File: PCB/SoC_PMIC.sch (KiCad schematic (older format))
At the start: 21 parts

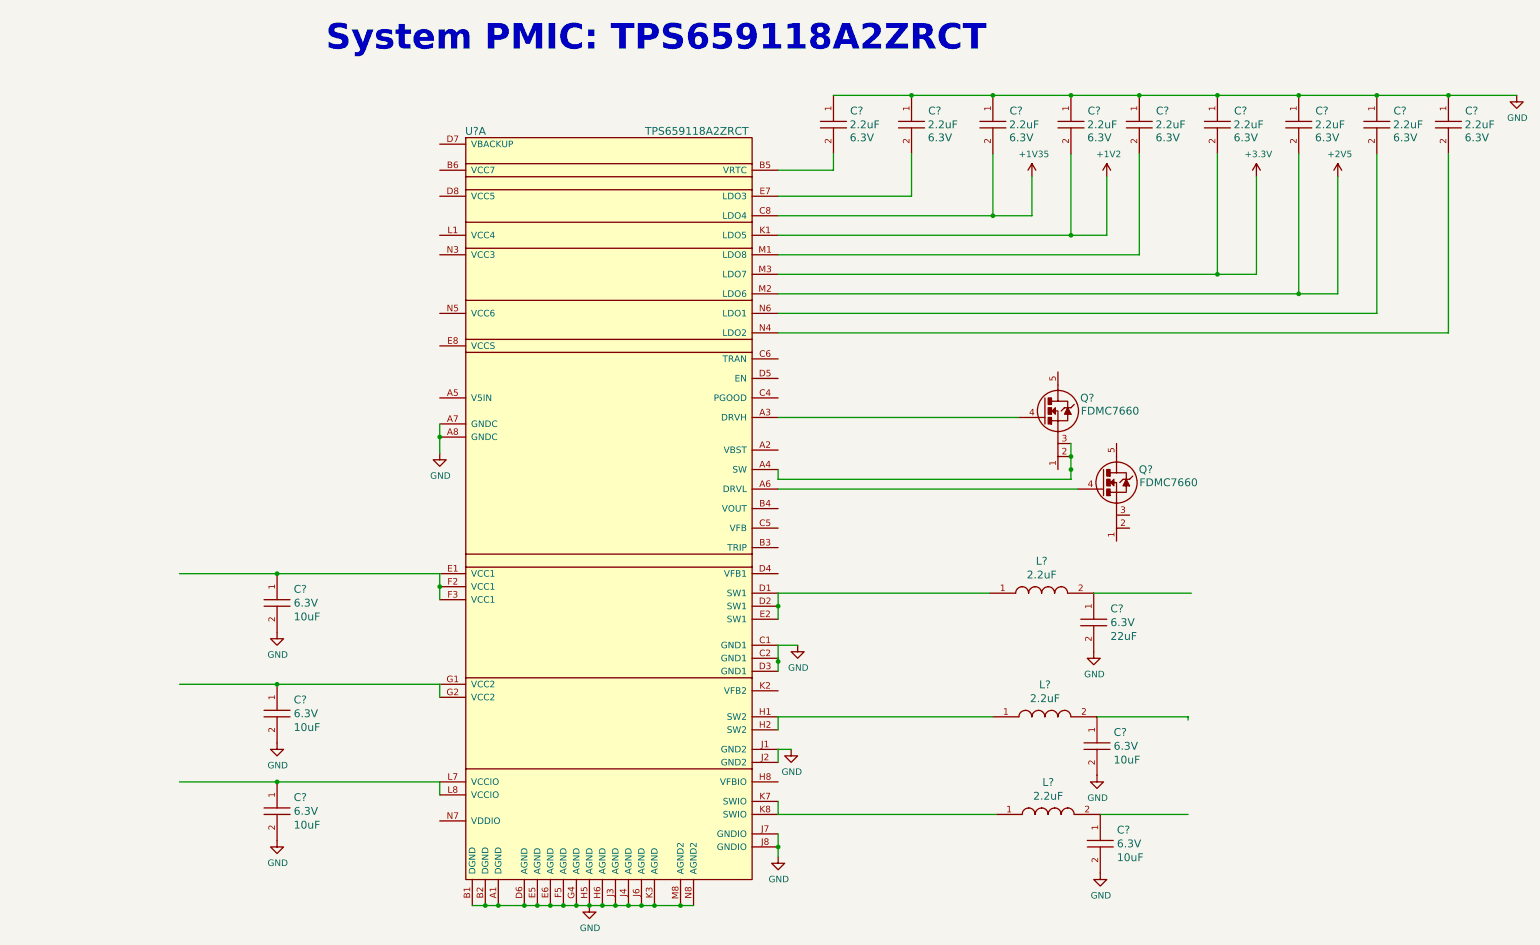
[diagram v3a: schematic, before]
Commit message: PMIC progress
More progress made on the implemenation of the PMIC schematic from the
Ti reference notes. Currently researching a 5V DCDC and input power
circuit that can switch between USB bus power and external power.
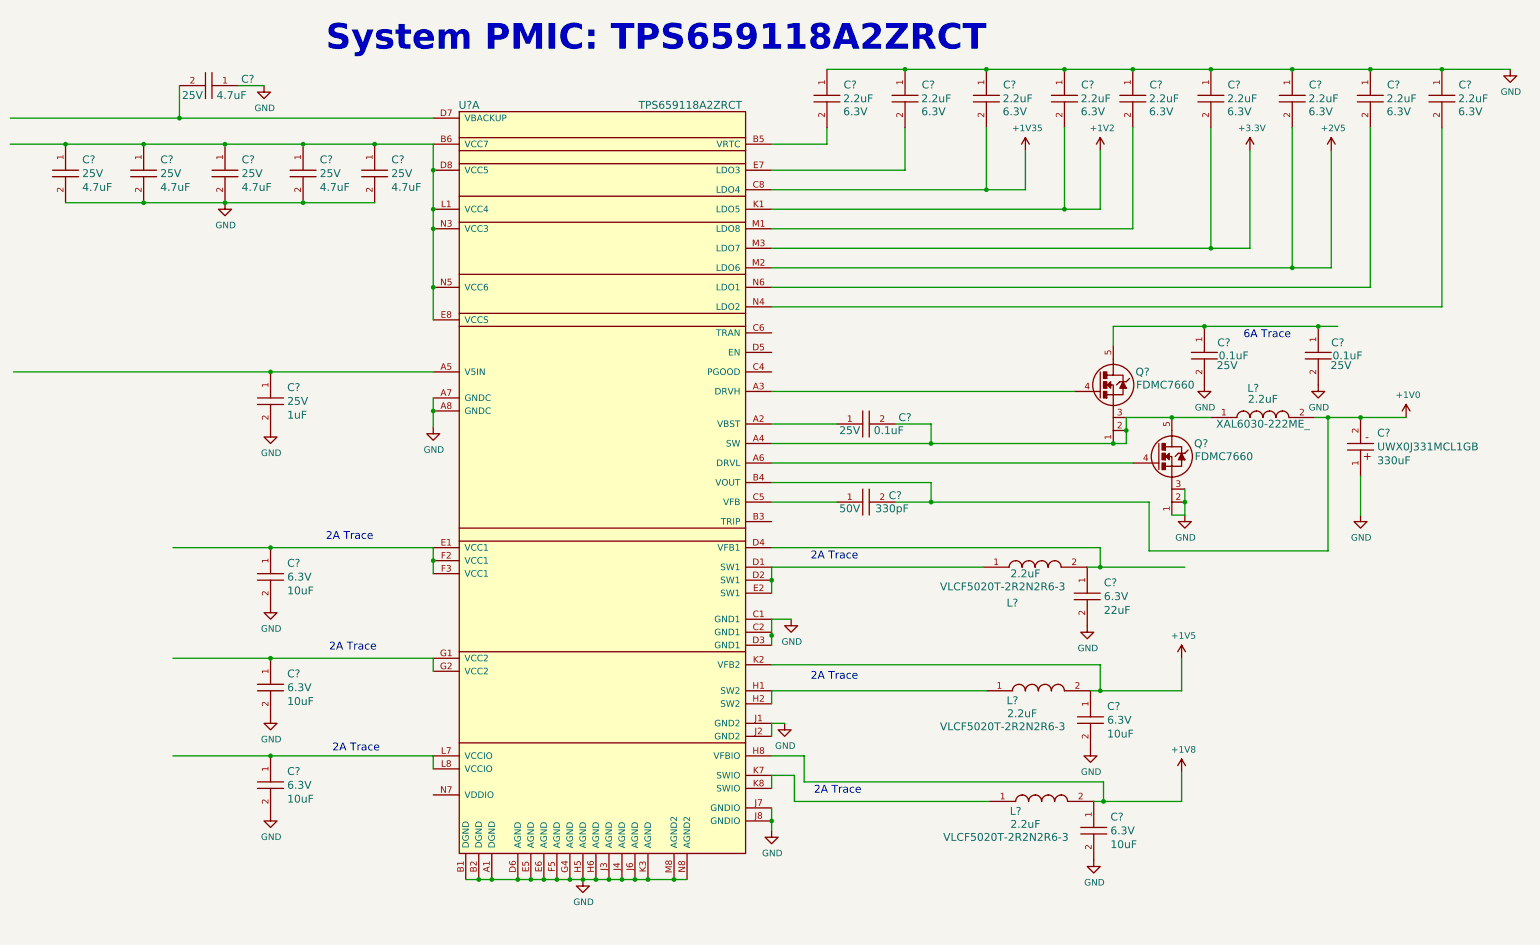
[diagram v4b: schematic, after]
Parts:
- added C? (x3): 08053C104JAT2A, PCB_Footprints:C0805, symbol 08053C104JAT2A
- added C?: GRM1555C1H331FA01J, PCB_Footprints:C0402, symbol GRM1555C1H331FA01J
- added C?: UWX0J331MCL1GB, PCB_Footprints:UWX0J331MCL1GB, symbol UWX0J331MCL1GB
- added C? (x6): CL05A475KQ5NRNC, PCB_Footprints:C0402, symbol CL05A475KQ5NRNC
- added C?: CL05A105KA5NQNC, PCB_Footprints:C0402, symbol CL05A105KA5NQNC
- added L?: XAL6030-222ME_, PCB_Footprints:XAL6030-222ME_, symbol XAL6030-222ME_
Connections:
- net labels added: +1V0, +1V5, +1V8
- wire segments 89 -> 86
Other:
- note added: "2A Trace"
- note added: "6A Trace"
- moved on the sheet: C?, L?, Q?, U?A

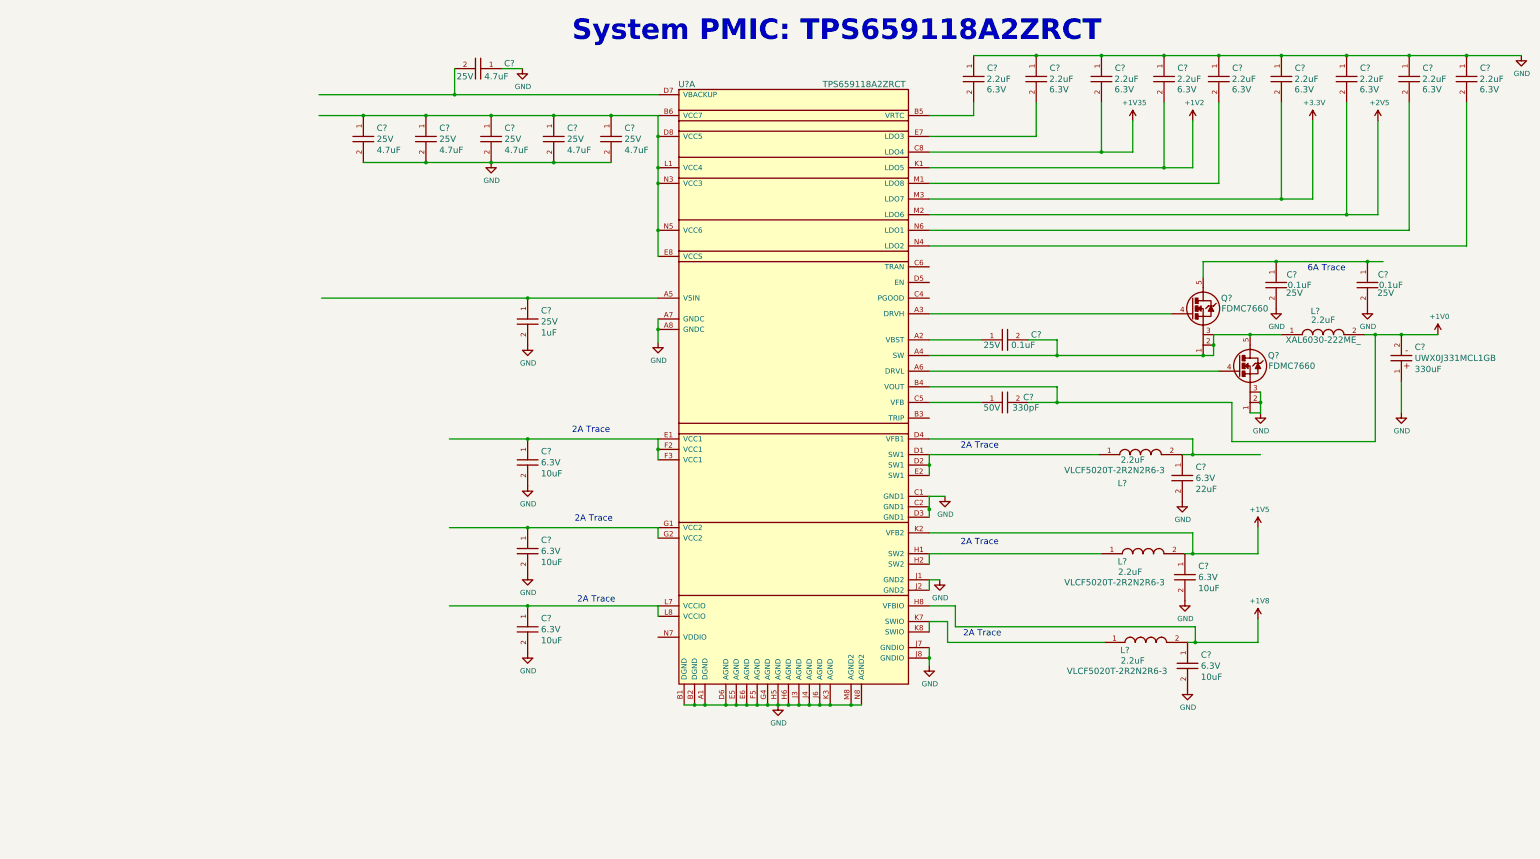
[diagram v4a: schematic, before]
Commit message: Schematic Progress
More progress on schematic. Image sensor schematic nearly finished, need
to check termination requirements of signals. Memory schematic nearly
solidified. LDO added to image sensor circuit for analog supply (3V).
Need to research termination requirements for memory as well. Need to
check what internal termination if any resistors are available in the
Zynq soc.
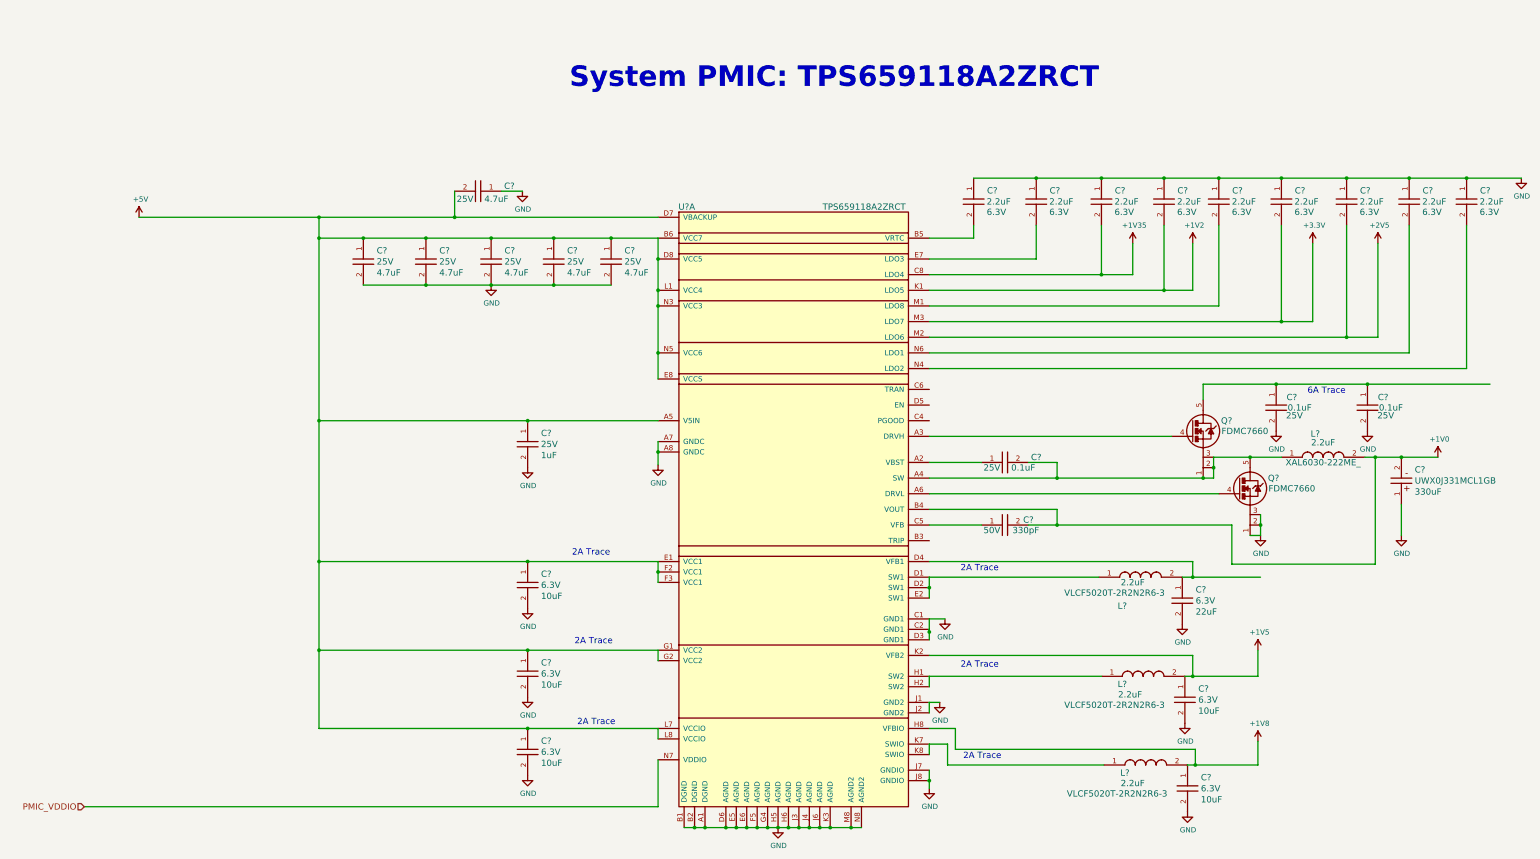
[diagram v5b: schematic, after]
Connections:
- net labels added: +5V, PMIC_VDDIO
- wire segments 86 -> 155
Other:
- moved on the sheet: C?, L?, Q?, U?A

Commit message: USB
This commit contains mostly work done to the USB sections. Theres a FTDI
chip for USB coms and programmign and an USB transceiver/PHY for usb
perfipherals or daisychaining devices.  Also the termiantion resistors
have been removed from the memory since termination can be set on DDR
pins of the FPGA with verilog.
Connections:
- net VCCPINT_1V0: now reaches C?.1, L?.2, U?.D4 (VFB1)
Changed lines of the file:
@@
 $Descr B 17000 11000
 encoding utf-8
-Sheet 7 8
+Sheet 7 10
 Title ""
 Date ""
@@
 $EndComp
 Wire Wire Line
-	6950 8425 7050 8425
-Wire Wire Line
-	7050 8425 7150 8425
-Wire Wire Line
-	7150 8425 7350 8425
-Wire Wire Line
-	7350 8425 7450 8425
-Wire Wire Line
-	7450 8425 7550 8425
-Wire Wire Line
-	7550 8425 7650 8425
-Wire Wire Line
-	7650 8425 7750 8425
-Wire Wire Line
-	7750 8425 7850 8425
-Wire Wire Line
-	7850 8425 7950 8425
-Wire Wire Line
-	7950 8425 8050 8425
-Wire Wire Line
-	8050 8425 8150 8425
-Wire Wire Line
-	8150 8425 8250 8425
-Wire Wire Line
-	8250 8425 8350 8425
-Wire Wire Line
-	8350 8425 8550 8425
-Wire Wire Line
-	8550 8425 8650 8425
+	6950 8425 8650 8425
 Connection ~ 7050 8425
 Connection ~ 7150 8425
@@
 Connection ~ 8550 8425
 Wire Wire Line
-	9300 7875 9300 7975
-Wire Wire Line
-	9300 7975 9300 8050
+	9300 7875 9300 8050
 Wire Wire Line
 	9300 7325 9300 7225
 Wire Wire Line
-	9300 6525 9300 6550
-Wire Wire Line
-	9300 6550 9300 6625
+	9300 6525 9300 6625
 Wire Wire Line
 	9300 6550 9300 6425
 Connection ~ 9300 6550
 Wire Wire Line
-	6700 4725 6700 4825
-Wire Wire Line
-	6700 4825 6700 4950
+	6700 4725 6700 4950
 $Comp
 L GND #PWR?
@@
 	9475 7825 10975 7825
 Wire Wire Line
-	9300 6025 9300 6125
-Wire Wire Line
-	9300 6125 9300 6225
+	9300 6025 9300 6225
 Connection ~ 9300 6125
 Wire Wire Line
 	9300 6025 10925 6025
 Wire Wire Line
-	12025 5075 11925 5075
-Wire Wire Line
-	11925 5075 10525 5075
-Wire Wire Line
-	10525 5075 9300 5075
+	12025 5075 9300 5075
 Text Notes 5850 1350 0    197  ~ 39
 System PMIC: TPS659118A2ZRCT
 Wire Wire Line
-	6700 5875 6700 5975
-Wire Wire Line
-	6700 5975 6700 6075
+	6700 5875 6700 6075
 Connection ~ 6700 5975
 Wire Wire Line
@@
 	6700 7475 6700 7575
 Wire Wire Line
-	3450 7475 5450 7475
-Wire Wire Line
-	5450 7475 6700 7475
-Wire Wire Line
-	3450 6725 5450 6725
-Wire Wire Line
-	5450 6725 6700 6725
-Wire Wire Line
-	3450 5875 5450 5875
-Wire Wire Line
-	5450 5875 6700 5875
+	3450 7475 6700 7475
+Wire Wire Line
+	3450 6725 6700 6725
+Wire Wire Line
+	3450 5875 6700 5875
 $Comp
 L CL10A225KQ8NNNC C?
@@
 	10325 2975 10325 2650
 Wire Wire Line
-	9300 3125 10950 3125
-Wire Wire Line
-	10950 3125 11250 3125
+	9300 3125 11250 3125
 Wire Wire Line
 	10950 3125 10950 2650
 Wire Wire Line
-	9300 3275 11550 3275
-Wire Wire Line
-	11550 3275 11825 3275
+	9300 3275 11825 3275
 Wire Wire Line
 	11550 3275 11550 2650
@@
 	12075 3425 12075 2650
 Wire Wire Line
-	9300 3575 12675 3575
-Wire Wire Line
-	12675 3575 12975 3575
+	9300 3575 12975 3575
 Wire Wire Line
 	12675 3575 12675 2650
 Wire Wire Line
-	9300 3725 13300 3725
-Wire Wire Line
-	13300 3725 13600 3725
+	9300 3725 13600 3725
 Wire Wire Line
 	13300 3725 13300 2650
@@
 	14450 4025 14450 2650
 Wire Wire Line
-	9725 2200 10325 2200
-Wire Wire Line
-	10325 2200 10950 2200
-Wire Wire Line
-	10950 2200 11550 2200
-Wire Wire Line
-	11550 2200 12075 2200
-Wire Wire Line
-	12075 2200 12675 2200
-Wire Wire Line
-	12675 2200 13300 2200
-Wire Wire Line
-	13300 2200 13900 2200
-Wire Wire Line
-	13900 2200 14450 2200
-Wire Wire Line
-	14450 2200 14975 2200
+	9725 2200 14975 2200
 Connection ~ 13900 2200
 Connection ~ 13300 2200
@@
 L GND #PWR?
 U 1 1 588BD4D5
-P 14975 2200
-F 0 "#PWR?" H 14975 1950 50  0001 C CNN
-F 1 "GND" H 14980 2027 50  0000 C CNN
-F 2 "" H 14975 2200 50  0001 C CNN
-F 3 "" H 14975 2200 50  0001 C CNN
-	1    14975 2200
+P 14975 2700
+F 0 "#PWR?" H 14975 2450 50  0001 C CNN
+F 1 "GND" H 14980 2527 50  0000 C CNN
+F 2 "" H 14975 2700 50  0001 C CNN
+F 3 "" H 14975 2700 50  0001 C CNN
+	1    14975 2700
 	1    0    0    -1
 $EndComp
@@
 $EndComp
 Wire Wire Line
-	11725 6025 11825 6025
-Wire Wire Line
-	11825 6025 12475 6025
-Wire Wire Line
-	11750 6975 11825 6975
-Wire Wire Line
-	11825 6975 12450 6975
-Wire Wire Line
-	11775 7825 11850 7825
-Wire Wire Line
-	11850 7825 12450 7825
+	11725 6025 15400 6025
+Wire Wire Line
+	11750 6975 12450 6975
+Wire Wire Line
+	11775 7825 12450 7825
 $Comp
 L GND #PWR?
@@
 	9300 5225 12075 5225
 Wire Wire Line
-	12025 4875 12025 4975
-Wire Wire Line
-	12025 4975 12025 5075
+	12025 4875 12025 5075
 Connection ~ 12025 4975
 Wire Wire Line
-	12025 4875 12375 4875
-Wire Wire Line
-	12375 4875 12675 4875
+	12025 4875 12675 4875
 Connection ~ 11925 5075
 Wire Wire Line
 	12475 5625 12375 5625
 Wire Wire Line
-	12475 5425 12475 5525
-Wire Wire Line
-	12475 5525 12475 5625
+	12475 5425 12475 5625
 Connection ~ 12475 5525
 $Comp
@@
 	10525 5375 10525 5525
 Wire Wire Line
-	10250 5525 10525 5525
-Wire Wire Line
-	10525 5525 12200 5525
+	10250 5525 12200 5525
 Wire Wire Line
 	12200 5525 12200 5900
@@
 	13575 5900 13575 4875
 Wire Wire Line
-	13475 4875 13575 4875
-Wire Wire Line
-	13575 4875 13825 4875
-Wire Wire Line
-	13825 4875 14175 4875
+	13475 4875 14175 4875
 $Comp
 L GRM1555C1H331FA01J C?
@@
 	11925 4325 11925 4175
 Wire Wire Line
-	11925 4175 12625 4175
-Wire Wire Line
-	12625 4175 13500 4175
-Wire Wire Line
-	13500 4175 14675 4175
+	11925 4175 14675 4175
 Connection ~ 12625 4175
 $Comp
@@
 $EndComp
 Wire Wire Line
-	6700 2775 6700 2975
-Wire Wire Line
-	6700 2975 6700 3275
-Wire Wire Line
-	6700 3275 6700 3425
-Wire Wire Line
-	6700 3425 6700 3875
-Wire Wire Line
-	6700 3875 6700 4125
+	6700 2775 6700 4125
 Connection ~ 6700 3275
 Connection ~ 6700 3425
@@
 Connection ~ 6700 2975
 Wire Wire Line
-	3450 2775 3875 2775
-Wire Wire Line
-	3875 2775 4475 2775
-Wire Wire Line
-	4475 2775 5100 2775
-Wire Wire Line
-	5100 2775 5700 2775
-Wire Wire Line
-	5700 2775 6250 2775
-Wire Wire Line
-	6250 2775 6700 2775
+	3450 2775 6700 2775
 Connection ~ 6250 2775
 Connection ~ 5700 2775
@@
 Connection ~ 4475 2775
 Wire Wire Line
-	3875 3225 4475 3225
-Wire Wire Line
-	4475 3225 5100 3225
-Wire Wire Line
-	5100 3225 5700 3225
-Wire Wire Line
-	5700 3225 6250 3225
+	3875 3225 6250 3225
 Connection ~ 4475 3225
 Connection ~ 5100 3225
@@
 $EndComp
 Wire Wire Line
-	3450 4525 5450 4525
-Wire Wire Line
-	5450 4525 6700 4525
+	3450 4525 6700 4525
 Connection ~ 5450 4525
 $Comp
@@
 $EndComp
 Wire Wire Line
-	1725 2575 3450 2575
-Wire Wire Line
-	3450 2575 4750 2575
-Wire Wire Line
-	4750 2575 6700 2575
+	1725 2575 6700 2575
 Wire Wire Line
 	4750 2325 4750 2575
@@
 	5400 2325 5200 2325
 Wire Wire Line
-	3450 2575 3450 2775
-Wire Wire Line
-	3450 2775 3450 4525
-Wire Wire Line
-	3450 4525 3450 5875
-Wire Wire Line
-	3450 5875 3450 6725
-Wire Wire Line
-	3450 6725 3450 7475
+	3450 2575 3450 7475
 Connection ~ 3450 2775
 Connection ~ 3450 4525
@@
 Text HLabel 1200 8225 0    60   Input ~ 0
 PMIC_VDDIO
+Text Label 13975 6025 0    60   ~ 0
+VCCPINT_1V0
+Text Notes 11425 5050 0    60   ~ 0
+6A Trace
+Text HLabel 15400 6025 2    60   Input ~ 0
+VCCPINT_1V0
+Wire Wire Line
+	14975 2200 14975 2700
 $EndSCHEMATC
